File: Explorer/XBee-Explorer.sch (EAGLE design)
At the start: 37 parts, among them U2 XBEE-1B3, U3 MIC5205 3.3V, U4 FT231XS, X1 USBSMD

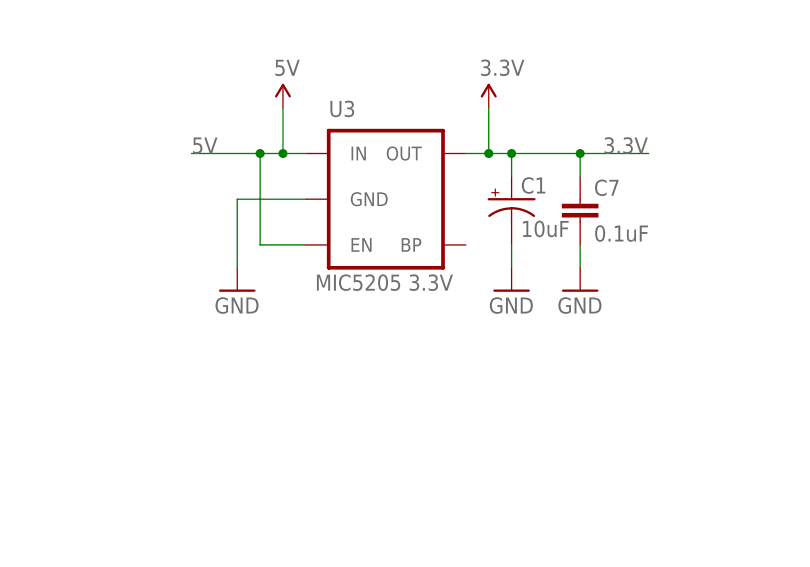
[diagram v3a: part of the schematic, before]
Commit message: Updating VREG part info on explorer
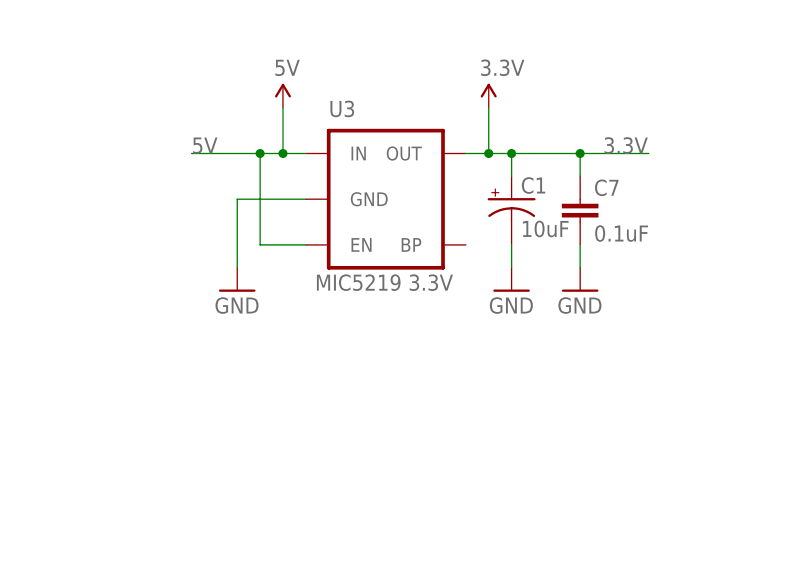
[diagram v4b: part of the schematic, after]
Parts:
- U3: value MIC5205 3.3V -> MIC5219 3.3V
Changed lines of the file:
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@@
 <grid distance="0.1" unitdist="inch" unit="inch" style="lines" multiple="1" display="no" altdistance="0.01" altunitdist="inch" altunit="inch"/>
 <layers>
-<layer number="1" name="Top" color="4" fill="1" visible="yes" active="no"/>
-<layer number="2" name="Route2" color="1" fill="3" visible="yes" active="no"/>
-<layer number="3" name="Route3" color="4" fill="3" visible="yes" active="no"/>
-<layer number="4" name="Route4" color="1" fill="4" visible="yes" active="no"/>
-<layer number="5" name="Route5" color="4" fill="4" visible="yes" active="no"/>
-<layer number="6" name="Route6" color="1" fill="8" visible="yes" active="no"/>
-<layer number="7" name="Route7" color="4" fill="8" visible="yes" active="no"/>
-<layer number="8" name="Route8" color="1" fill="2" visible="yes" active="no"/>
-<layer number="9" name="Route9" color="4" fill="2" visible="yes" active="no"/>
-<layer number="10" name="Route10" color="1" fill="7" visible="yes" active="no"/>
-<layer number="11" name="Route11" color="4" fill="7" visible="yes" active="no"/>
-<layer number="12" name="Route12" color="1" fill="5" visible="yes" active="no"/>
-<layer number="13" name="Route13" color="4" fill="5" visible="yes" active="no"/>
-<layer number="14" name="Route14" color="1" fill="6" visible="yes" active="no"/>
-<layer number="15" name="Route15" color="4" fill="6" visible="yes" active="no"/>
-<layer number="16" name="Bottom" color="1" fill="1" visible="yes" active="no"/>
-<layer number="17" name="Pads" color="2" fill="1" visible="yes" active="no"/>
-<layer number="18" name="Vias" color="2" fill="1" visible="yes" active="no"/>
-<layer number="19" name="Unrouted" color="6" fill="1" visible="yes" active="no"/>
-<layer number="20" name="Dimension" color="15" fill="1" visible="yes" active="no"/>
-<layer number="21" name="tPlace" color="16" fill="1" visible="yes" active="no"/>
-<layer number="22" name="bPlace" color="14" fill="1" visible="yes" active="no"/>
-<layer number="23" name="tOrigins" color="15" fill="1" visible="yes" active="no"/>
-<layer number="24" name="bOrigins" color="15" fill="1" visible="yes" active="no"/>
-<layer number="25" name="tNames" color="7" fill="1" visible="yes" active="no"/>
-<layer number="26" name="bNames" color="7" fill="1" visible="yes" active="no"/>
-<layer number="27" name="tValues" color="7" fill="1" visible="yes" active="no"/>
-<layer number="28" name="bValues" color="7" fill="1" visible="yes" active="no"/>
+<layer number="1" name="Top" color="4" fill="1" visible="no" active="no"/>
+<layer number="2" name="Route2" color="1" fill="3" visible="no" active="no"/>
+<layer number="3" name="Route3" color="4" fill="3" visible="no" active="no"/>
+<layer number="4" name="Route4" color="1" fill="4" visible="no" active="no"/>
+<layer number="5" name="Route5" color="4" fill="4" visible="no" active="no"/>
+<layer number="6" name="Route6" color="1" fill="8" visible="no" active="no"/>
+<layer number="7" name="Route7" color="4" fill="8" visible="no" active="no"/>
+<layer number="8" name="Route8" color="1" fill="2" visible="no" active="no"/>
+<layer number="9" name="Route9" color="4" fill="2" visible="no" active="no"/>
+<layer number="10" name="Route10" color="1" fill="7" visible="no" active="no"/>
+<layer number="11" name="Route11" color="4" fill="7" visible="no" active="no"/>
+<layer number="12" name="Route12" color="1" fill="5" visible="no" active="no"/>
+<layer number="13" name="Route13" color="4" fill="5" visible="no" active="no"/>
+<layer number="14" name="Route14" color="1" fill="6" visible="no" active="no"/>
+<layer number="15" name="Route15" color="4" fill="6" visible="no" active="no"/>
+<layer number="16" name="Bottom" color="1" fill="1" visible="no" active="no"/>
+<layer number="17" name="Pads" color="2" fill="1" visible="no" active="no"/>
+<layer number="18" name="Vias" color="2" fill="1" visible="no" active="no"/>
+<layer number="19" name="Unrouted" color="6" fill="1" visible="no" active="no"/>
+<layer number="20" name="Dimension" color="15" fill="1" visible="no" active="no"/>
+<layer number="21" name="tPlace" color="16" fill="1" visible="no" active="no"/>
+<layer number="22" name="bPlace" color="14" fill="1" visible="no" active="no"/>
+<layer number="23" name="tOrigins" color="15" fill="1" visible="no" active="no"/>
+<layer number="24" name="bOrigins" color="15" fill="1" visible="no" active="no"/>
+<layer number="25" name="tNames" color="7" fill="1" visible="no" active="no"/>
+<layer number="26" name="bNames" color="7" fill="1" visible="no" active="no"/>
+<layer number="27" name="tValues" color="7" fill="1" visible="no" active="no"/>
+<layer number="28" name="bValues" color="7" fill="1" visible="no" active="no"/>
 <layer number="29" name="tStop" color="7" fill="3" visible="no" active="no"/>
 <layer number="30" name="bStop" color="7" fill="6" visible="no" active="no"/>
@@
 <layer number="35" name="tGlue" color="7" fill="4" visible="no" active="no"/>
 <layer number="36" name="bGlue" color="7" fill="5" visible="no" active="no"/>
-<layer number="37" name="tTest" color="7" fill="1" visible="yes" active="no"/>
-<layer number="38" name="bTest" color="7" fill="1" visible="yes" active="no"/>
+<layer number="37" name="tTest" color="7" fill="1" visible="no" active="no"/>
+<layer number="38" name="bTest" color="7" fill="1" visible="no" active="no"/>
 <layer number="39" name="tKeepout" color="4" fill="11" visible="no" active="no"/>
 <layer number="40" name="bKeepout" color="1" fill="11" visible="no" active="no"/>
@@
 <layer number="44" name="Drills" color="7" fill="1" visible="no" active="no"/>
 <layer number="45" name="Holes" color="7" fill="1" visible="no" active="no"/>
-<layer number="46" name="Milling" color="3" fill="1" visible="yes" active="no"/>
-<layer number="47" name="Measures" color="7" fill="1" visible="yes" active="no"/>
-<layer number="48" name="Document" color="7" fill="1" visible="yes" active="no"/>
-<layer number="49" name="Reference" color="7" fill="1" visible="yes" active="no"/>
-<layer number="50" name="dxf" color="7" fill="1" visible="yes" active="no"/>
-<layer number="51" name="tDocu" color="6" fill="1" visible="yes" active="no"/>
-<layer number="52" name="bDocu" color="7" fill="1" visible="yes" active="no"/>
-<layer number="53" name="tGND_GNDA" color="7" fill="9" visible="yes" active="no"/>
-<layer number="54" name="bGND_GNDA" color="1" fill="9" visible="yes" active="no"/>
-<layer number="56" name="wert" color="7" fill="1" visible="yes" active="no"/>
+<layer number="46" name="Milling" color="3" fill="1" visible="no" active="no"/>
+<layer number="47" name="Measures" color="7" fill="1" visible="no" active="no"/>
+<layer number="48" name="Document" color="7" fill="1" visible="no" active="no"/>
+<layer number="49" name="Reference" color="7" fill="1" visible="no" active="no"/>
+<layer number="50" name="dxf" color="7" fill="1" visible="no" active="no"/>
+<layer number="51" name="tDocu" color="6" fill="1" visible="no" active="no"/>
+<layer number="52" name="bDocu" color="7" fill="1" visible="no" active="no"/>
+<layer number="53" name="tGND_GNDA" color="7" fill="9" visible="no" active="no"/>
+<layer number="54" name="bGND_GNDA" color="1" fill="9" visible="no" active="no"/>
+<layer number="56" name="wert" color="7" fill="1" visible="no" active="no"/>
 <layer number="91" name="Nets" color="2" fill="1" visible="yes" active="yes"/>
 <layer number="92" name="Busses" color="1" fill="1" visible="yes" active="yes"/>
@@
 <part name="GND4" library="SparkFun" deviceset="GND" device=""/>
 <part name="P+2" library="SparkFun" deviceset="3.3V" device=""/>
-<part name="U3" library="SparkFun" deviceset="V_REG_LDO" device="SMD" value="MIC5205 3.3V"/>
+<part name="U3" library="SparkFun" deviceset="V_REG_LDO" device="SMD" value="MIC5219 3.3V"/>
 <part name="GND1" library="SparkFun" deviceset="GND" device=""/>
 <part name="C1" library="SparkFun" deviceset="CAP_POL" device="1206" value="10uF"/>
